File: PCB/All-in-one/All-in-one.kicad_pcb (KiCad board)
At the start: 2 copper layers, 4 parts, among them U1 MPU6050, U2 BMP280, U3 NEO-6M-GPS, U4 STM32F401CCUx

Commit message: Updated PCB Layout
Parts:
- added C1: 10u, Capacitor_SMD:C_1206_3216Metric, F.Cu at (161.7, 63.9)
- added C10: 1u, Capacitor_SMD:C_0603_1608Metric, F.Cu at (134.9, 64.2)
- added C11: 10n, Capacitor_SMD:C_0402_1005Metric, F.Cu at (133.5, 64.4)
- added C12: 4u7, Capacitor_SMD:C_0603_1608Metric, F.Cu at (134.6, 55.3)
- added C13: 100n, Capacitor_SMD:C_0402_1005Metric, F.Cu at (135.1, 57.2)
- added C14: 100n, Capacitor_SMD:C_0402_1005Metric, F.Cu at (143.5, 65.3)
- added C15: 100n, Capacitor_SMD:C_0402_1005Metric, F.Cu at (144.8, 56.9)
- added C16: 100n, Capacitor_SMD:C_0402_1005Metric, F.Cu at (137.3, 55.6)
- added C17: 12p, Capacitor_SMD:C_0402_1005Metric, F.Cu at (131.8, 57.0)
- added C18: 12p, Capacitor_SMD:C_0402_1005Metric, F.Cu at (131.9, 62.6)
- added C19: 4u7, Capacitor_SMD:C_0603_1608Metric, F.Cu at (141.7, 66.4)
- added C2: 100n, Capacitor_SMD:C_0805_2012Metric, F.Cu at (164.3, 63.9)
- added C20: 10u, Capacitor_SMD:C_0603_1608Metric, F.Cu at (134.5, 43.4)
- added C21: 100n, Capacitor_SMD:C_0402_1005Metric, F.Cu at (134.5, 44.8)
- added C22: 10n, Capacitor_SMD:C_0402_1005Metric, F.Cu at (144.3, 48.8)
- added C23: 100n, Capacitor_SMD:C_0402_1005Metric, F.Cu at (141.5, 44.1)
- added C24: 100n, Capacitor_SMD:C_0402_1005Metric, F.Cu at (144.3, 46.2)
- added C25: 2n2, Capacitor_SMD:C_0402_1005Metric, F.Cu at (137.5, 46.1)
- added C26: 10u, Capacitor_SMD:C_0805_2012Metric, F.Cu at (158.1, 78.8)
- added C27: 10u, Capacitor_SMD:C_0805_2012Metric, F.Cu at (151.7, 76.5)
- added C28: 10u, Capacitor_SMD:C_0805_2012Metric, F.Cu at (154.7, 54.6)
- added C3: 100n, Capacitor_SMD:C_0805_2012Metric, F.Cu at (168.1, 60.6)
- added C4: 22u, Capacitor_SMD:C_1206_3216Metric, F.Cu at (161.5, 58.6)
- added C5: 22u, Capacitor_SMD:C_1206_3216Metric, F.Cu at (164.3, 58.6)
- added C6: 10u, Capacitor_SMD:C_1206_3216Metric, F.Cu at (164.5, 81.2)
- added C7: 100n, Capacitor_SMD:C_0805_2012Metric, F.Cu at (162.1, 80.6)
- added C8: 100n, Capacitor_SMD:C_0805_2012Metric, F.Cu at (159.1, 81.8)
- added C9: 100n, Capacitor_SMD:C_0402_1005Metric, F.Cu at (134.8, 61.6)
- added D1: B5819W, Diode_SMD:D_SOD-123, F.Cu at (157.9, 70.0)
- added D2: LED_BLUE, LED_SMD:LED_0603_1608Metric, F.Cu at (156.1, 76.2)
- added D3: LED_RED, LED_SMD:LED_0603_1608Metric, F.Cu at (159.1, 53.9)
- added D4: LED_GREEN, LED_SMD:LED_0402_1005Metric, F.Cu at (128.8, 24.5)
- added F1: 250mA, Fuse:Fuse_1206_3216Metric, F.Cu at (167.1, 68.2)
- added F2: 250mA, Fuse:Fuse_1206_3216Metric, F.Cu at (162.3, 77.5)
- added FB1: 600 @ 600MHz, Inductor_SMD:L_1206_3216Metric, F.Cu at (163.3, 67.5)
- added H1: MountingHole_Pad, MountingHole:MountingHole_3.5mm_Pad_Via, F.Cu at (189.0, 29.4)
- added H2: MountingHole_Pad, MountingHole:MountingHole_3.5mm_Pad_Via, F.Cu at (166.1, 29.4)
- added H3: MountingHole_Pad, MountingHole:MountingHole_3.5mm_Pad_Via, F.Cu at (177.5, 29.4)
- added H4: MountingHole_Pad, MountingHole:MountingHole_3.5mm_Pad_Via, F.Cu at (200.4, 29.4)
- added J1: HIGH VOLTAGE, TerminalBlock_TE-Connectivity:TerminalBlock_TE_282834-2_1x02_P2.54mm_Horizontal, F.Cu at (176.5, 68.2)
- added J10: SWD, Connector_PinHeader_2.54mm:PinHeader_2x05_P2.54mm_Vertical, F.Cu at (96.2, 63.1)
- added J2: LOW VOLTAGE, TerminalBlock_TE-Connectivity:TerminalBlock_TE_282834-2_1x02_P2.54mm_Horizontal, F.Cu at (169.9, 79.0)
- added J3: Micro_SD_Card_Det, All-in-one-custom:SD_Card_custom, F.Cu at (132.3, 72.6)
- added J4: USB_C_Receptacle_USB2.0, All-in-one-custom:USB_C_16PIN, F.Cu at (152.6, 45.8)
- added J5: GPIO, Connector_PinHeader_2.54mm:PinHeader_1x04_P2.54mm_Vertical, F.Cu at (104.5, 82.0)
- added J6: Conn_01x02, Connector_PinHeader_2.54mm:PinHeader_1x02_P2.54mm_Vertical, F.Cu at (107.0, 74.4)
- added J7: Conn_01x02, Connector_PinHeader_2.54mm:PinHeader_1x02_P2.54mm_Vertical, F.Cu at (107.0, 79.5)
- added J8: I2C_EXT, Connector_PinHeader_2.54mm:PinHeader_1x04_P2.54mm_Vertical, F.Cu at (153.4, 22.1)
- added J9: UART_EXT, Connector_PinHeader_2.54mm:PinHeader_1x04_P2.54mm_Vertical, F.Cu at (110.8, 70.6)
- added L1: 2u2, All-in-one-custom:SMNR4020-2.2UH, F.Cu at (157.7, 63.8)
- added L2: 39n, Inductor_SMD:L_0402_1005Metric, F.Cu at (132.4, 64.5)
- added Q1: AO3401A, Package_TO_SOT_SMD:SOT-23, F.Cu at (170.5, 68.2)
- added R1: 33k, Resistor_SMD:R_0603_1608Metric, F.Cu at (170.5, 58.5)
- added R10: 2k2, Resistor_SMD:R_0603_1608Metric, F.Cu at (141.5, 52.9)
- added R11: 10k, Resistor_SMD:R_0402_1005Metric, F.Cu at (127.1, 73.0)
- added R12: 5k1, Resistor_SMD:R_0402_1005Metric, F.Cu at (150.8, 47.8)
- added R13: 5k1, Resistor_SMD:R_0402_1005Metric, F.Cu at (155.8, 47.8)
- added R14: 10k, Resistor_SMD:R_0603_1608Metric, F.Cu at (155.5, 81.7)
- added R15: 13k, Resistor_SMD:R_0603_1608Metric, F.Cu at (151.9, 80.8)
- added R16: 1k, Resistor_SMD:R_0603_1608Metric, F.Cu at (156.7, 53.0)
- added R17: 10k, Resistor_SMD:R_0603_1608Metric, F.Cu at (157.9, 59.0)
- added R18: 13k, Resistor_SMD:R_0603_1608Metric, F.Cu at (154.9, 58.0)
- added R2: 200, Resistor_SMD:R_0603_1608Metric, F.Cu at (171.2, 61.2)
- added R3: 10k, Resistor_SMD:R_0603_1608Metric, F.Cu at (171.2, 64.7)
- added R4: 1k5, Resistor_SMD:R_0603_1608Metric, F.Cu at (153.7, 75.5)
- added R5: 10k, Resistor_SMD:R_0402_1005Metric, F.Cu at (137.3, 54.4)
- added R6: 510, Resistor_SMD:R_0402_1005Metric, F.Cu at (134.8, 60.4)
- added R7: 1k, Resistor_SMD:R_0603_1608Metric, F.Cu at (136.6, 27.3)
- added R8: 10k, Resistor_SMD:R_0402_1005Metric, F.Cu at (117.3, 81.4)
- added R9: 2k2, Resistor_SMD:R_0603_1608Metric, F.Cu at (138.2, 52.9)
- added SW1: SW_DP3T, All-in-one-custom:K3-2336D-F1, F.Cu at (169.9, 75.0)
- added SW2: SW_Push, All-in-one-custom:GT-TC029, F.Cu at (124.7, 63.3)
- added SW3: SW_Push, All-in-one-custom:GT-TC029, F.Cu at (121.1, 70.4)
- added U5: MPU-6050, Sensor_Motion:InvenSense_QFN-24_4x4mm_P0.5mm, F.Cu at (140.9, 47.5)
- added U6: USBLC6-2P6, Package_TO_SOT_SMD:SOT-666, F.Cu at (153.4, 49.2)
- added U7: MT9700, Package_TO_SOT_SMD:SOT-23-5, F.Cu at (154.9, 78.8)
- added U8: MT9700, Package_TO_SOT_SMD:SOT-23-5, F.Cu at (157.9, 56.5)
- added Y1: 25MHz 12pF, Crystal:Crystal_SMD_3225-4Pin_3.2x2.5mm, F.Cu at (131.9, 59.9)
- U1: value MPU6050 -> TPS563201DDCR; footprint MPU:IC_MPU6050 -> Package_TO_SOT_SMD:SOT-23-6
- U2: value BMP280 -> NCP114AMX330TCG; footprint BMP:XDCR_BMP280 -> Package_DFN_QFN:UDFN-4-1EP_1x1mm_P0.65mm_EP0.48x0.48mm
- U3: value NEO-6M-GPS -> STM32F401CDUx; footprint NEO6M:XCVR_NEO-6M-GPS -> Package_DFN_QFN:QFN-48-1EP_7x7mm_P0.5mm_EP5.6x5.6mm
- U4: value STM32F401CCUx -> BMP280; footprint Package_DFN_QFN:QFN-48-1EP_7x7mm_P0.5mm_EP5.6x5.6mm -> Package_LGA:Bosch_LGA-8_2x2.5mm_P0.65mm_ClockwisePinNumbering
- moved U1 72.3 mm to (167.9, 63.9)
- moved U2 65.0 mm to (160.1, 79.8), turned to 90 degrees
- moved U4 44.8 mm to (134.7, 46.8), turned to 180 degrees
- moved U3 18.3 mm to (140.0, 60.4)
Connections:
- U1 pad 1: unconnected-(U1-Pad1) -> GND
- U1 pad 2: unconnected-(U1-Pad2) -> BUCK_SW
- U1 pad 3: unconnected-(U1-Pad3) -> Net-(C2-Pad1)
- U1 pad 4: unconnected-(U1-Pad4) -> BUCK_VFB
- U1 pad 5: unconnected-(U1-Pad5) -> Net-(C2-Pad1)
- U1 pad 6: unconnected-(U1-Pad6) -> BUCK_VBST
- U2 pad 1: Net-(U2-Pad1) -> Net-(C8-Pad1)
- U2 pad 2: unconnected-(U2-Pad2) -> GND
- U2 pad 3: unconnected-(U2-Pad3) -> Net-(U2-Pad3)
- U2 pad 4: unconnected-(U2-Pad4) -> Net-(U2-Pad3)
- U2 pad 5: unconnected-(U2-Pad5) -> (no net)
- U3 pad 1: (no net) -> +3.3V
- U3 pad 10: Net-(U3-Pad10) -> TIM2_CH1
- U3 pad 12: Net-(U3-Pad10) -> TIM5_CH1
- U3 pad 13: Net-(U3-Pad10) -> unconnected-(U3-Pad13)
- U3 pad 14: unconnected-(U3-Pad14) -> SPI1_NSS
- U3 pad 15: unconnected-(U3-Pad15) -> SPI1_SCK
- U3 pad 16: unconnected-(U3-Pad16) -> SPI1_MISO
- U3 pad 17: unconnected-(U3-Pad17) -> SPI1_MOSI
- U3 pad 18: unconnected-(U3-Pad18) -> SD_CARD_DET
- U3 pad 20: unconnected-(U3-Pad20) -> LED_STATUS
- U3 pad 22: unconnected-(U3-Pad22) -> Net-(C19-Pad1)
- U3 pad 23: unconnected-(U3-Pad23) -> GND
- U3 pad 24: Net-(U3-Pad10) -> +3.3V
- U3 pad 5: unconnected-(U3-Pad5) -> HSE_IN
- U3 pad 6: unconnected-(U3-Pad6) -> HSE_OUT
- U3 pad 7: unconnected-(U3-Pad7) -> NRST
- U3 pad 8: unconnected-(U3-Pad8) -> GND
- U3 pad 9: unconnected-(U3-Pad9) -> +3.3VA
- U4 pad 1: unconnected-(U4-Pad1) -> GND
- U4 pad 2: unconnected-(U4-Pad2) -> +3.3V
- U4 pad 3: unconnected-(U4-Pad3) -> I2C1_SDA
- U4 pad 4: unconnected-(U4-Pad4) -> I2C1_SCL
- U4 pad 5: unconnected-(U4-Pad5) -> GND
- U4 pad 6: unconnected-(U4-Pad6) -> +3.3V
- U4 pad 7: unconnected-(U4-Pad7) -> GND
- U4 pad 8: unconnected-(U4-Pad8) -> +3.3V
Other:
- copper layers 2 -> 4

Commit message: Recovery File
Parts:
- moved D1 16.6 mm to (151.9, 54.6), turned to 90 degrees
- moved U6 0.80 mm to (152.9, 48.6)
- moved R12 0.40 mm to (150.4, 47.8)
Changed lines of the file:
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@@
   )
   (footprint "Package_TO_SOT_SMD:SOT-666" (layer "F.Cu")
-    (at 153.4 49.225 -90)
+    (at 152.9 48.6 -90)
     (descr "SOT666")
     (tags "SOT-666")
@@
       (effects (font (size 1 1) (thickness 0.15)))
     )
-    (fp_rect (start -0.3 0.3) (end 13.1 13.2) (layer "F.SilkS") (width 0.2) (fill none))
+    (fp_rect (start -2.3 -1.6) (end 15.8 13.2) (layer "F.SilkS") (width 0.2) (fill none))
     (pad "" np_thru_hole circle (at 9.65 10.5) (size 0.8 0.8) (drill 0.8) (layers F&B.Cu *.Mask))
     (pad "" np_thru_hole circle (at 1.65 10.5) (size 0.8 0.8) (drill 0.8) (layers F&B.Cu *.Mask))
@@
   )
   (footprint "Resistor_SMD:R_0402_1005Metric" (layer "F.Cu")
-    (at 150.8 47.825 180)
+    (at 150.4 47.825 180)
     (descr "Resistor SMD 0402 (1005 Metric), square (rectangular) end terminal, IPC_7351 nominal, (Body size source: IPC-SM-782 page 72, https://www.pcb-3d.com/wordpress/wp-content/uploads/ipc-sm-782a_amendment_1_and_2.pdf), generated with kicad-footprint-generator")
     (tags "resistor")
@@
   )
   (footprint "Diode_SMD:D_SOD-123" (layer "F.Cu")
-    (at 157.9375 70.05 180)
+    (at 151.9 54.6 90)
     (descr "SOD-123")
     (tags "SOD-123")
@@
     (property "Sheetname" "")
     (attr smd)
-    (fp_text reference "D1" (at 0 -2) (layer "F.SilkS")
-      (effects (font (size 1 1) (thickness 0.15)))
-    )
-    (fp_text value "B5819W" (at 0 2.1) (layer "F.Fab")
-      (effects (font (size 1 1) (thickness 0.15)))
-    )
-    (fp_text user "${REFERENCE}" (at 0 -2) (layer "F.Fab")
+    (fp_text reference "D1" (at 0 -2 90) (layer "F.SilkS")
+      (effects (font (size 1 1) (thickness 0.15)))
+    )
+    (fp_text value "B5819W" (at 0 2.1 90) (layer "F.Fab")
+      (effects (font (size 1 1) (thickness 0.15)))
+    )
+    (fp_text user "${REFERENCE}" (at 0 -2 90) (layer "F.Fab")
       (effects (font (size 1 1) (thickness 0.15)))
     )
@@
     (fp_line (start 0.25 -0.4) (end 0.25 0.4) (layer "F.Fab") (width 0.1))
     (fp_line (start -1.4 -0.9) (end 1.4 -0.9) (layer "F.Fab") (width 0.1))
-    (pad "1" smd rect (at -1.65 0 180) (size 0.9 1.2) (layers "F.Cu" "F.Paste" "F.Mask")
+    (pad "1" smd rect (at -1.65 0 90) (size 0.9 1.2) (layers "F.Cu" "F.Paste" "F.Mask")
       (net 82 "BUCK_VIN") (pinfunction "K") (pintype "passive"))
-    (pad "2" smd rect (at 1.65 0 180) (size 0.9 1.2) (layers "F.Cu" "F.Paste" "F.Mask")
+    (pad "2" smd rect (at 1.65 0 90) (size 0.9 1.2) (layers "F.Cu" "F.Paste" "F.Mask")
       (net 18 "+5V") (pinfunction "A") (pintype "passive"))
     (model "${KICAD6_3DMODEL_DIR}/Diode_SMD.3dshapes/D_SOD-123.wrl"

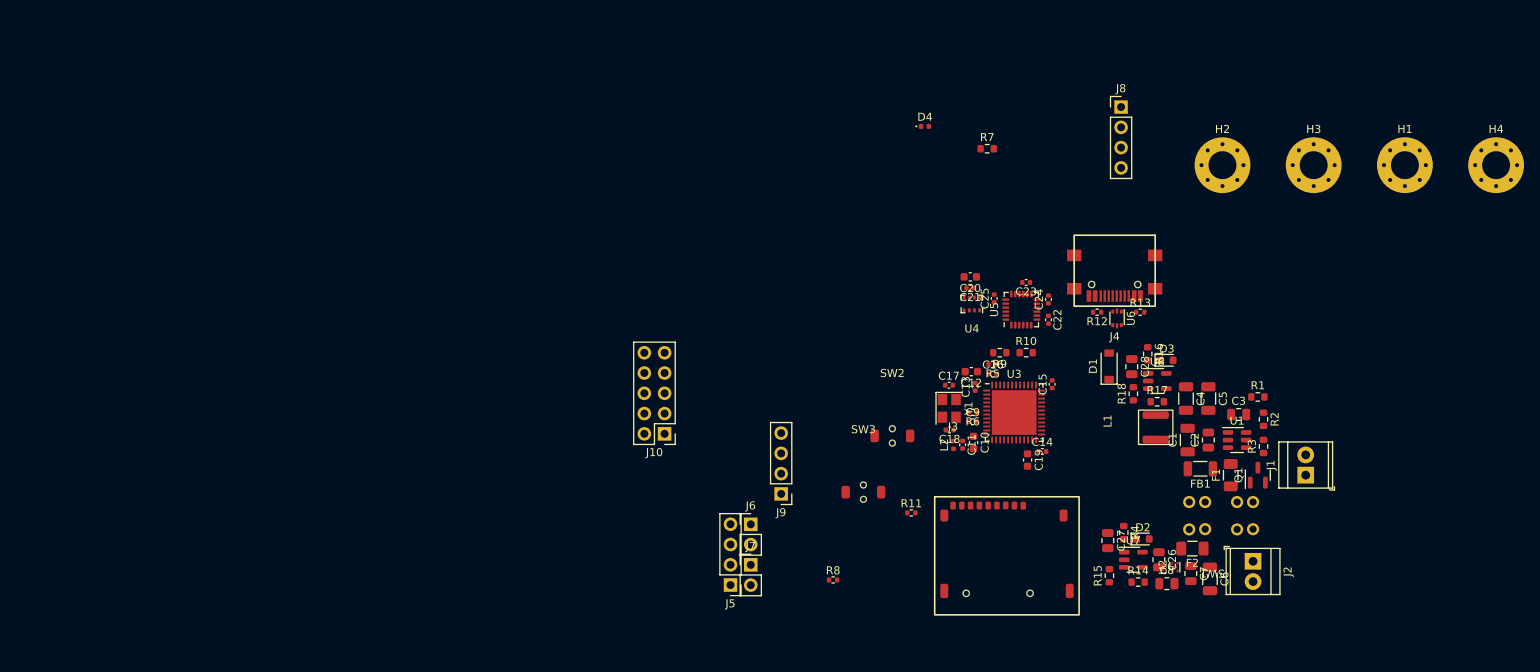
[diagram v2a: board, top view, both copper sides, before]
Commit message: Completed PCB Layout (No Tracing) - Made PCB layout - Tracing need to be done
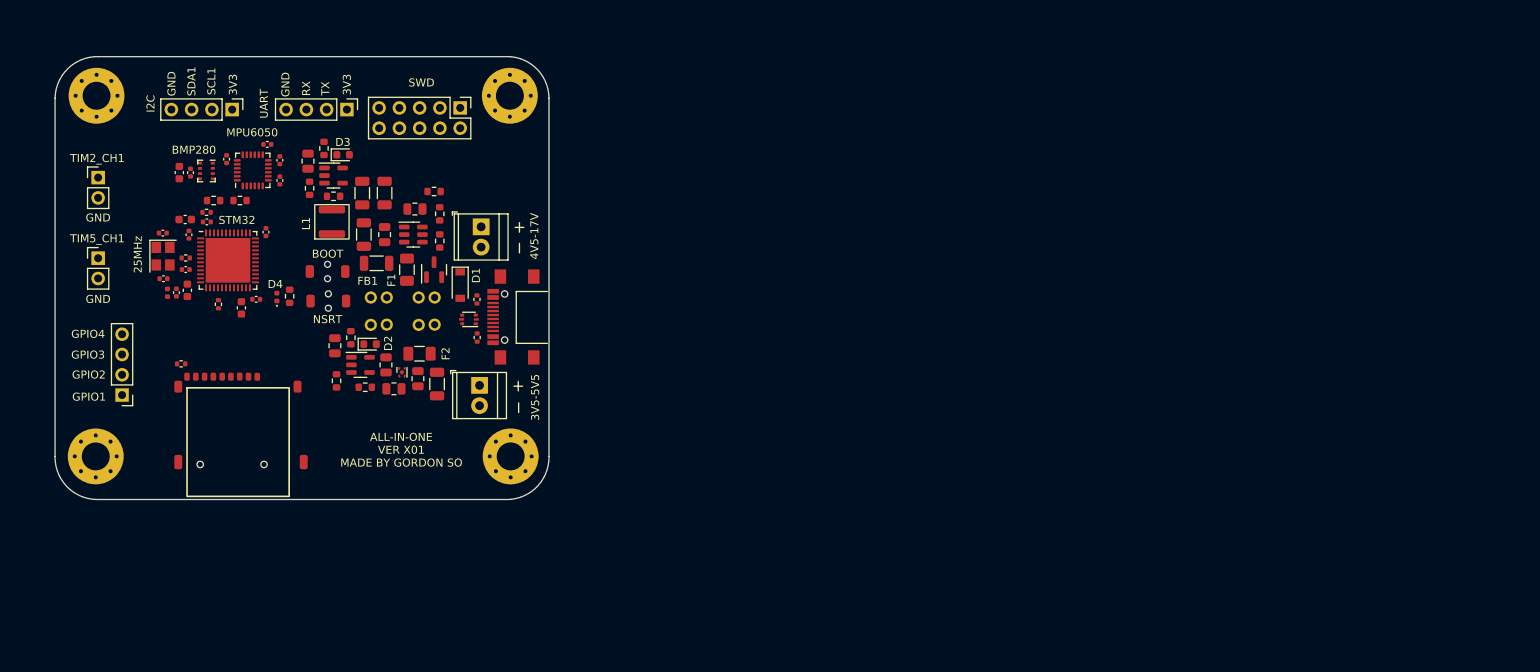
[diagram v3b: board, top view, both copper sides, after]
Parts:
- J5: value GPIO -> GPIO1
- J6: value Conn_01x02 -> TIM2_CH1
- J7: value Conn_01x02 -> TIM5_CH1
- J8: value I2C_EXT -> I2C
- J9: value UART_EXT -> UART
- U5: value MPU-6050 -> MPU6050
- moved H3 156.9 mm to (24.9, 65.9)
- moved H2 141.4 mm to (25.0, 20.7)
- moved H4 128.8 mm to (76.9, 65.9)
- moved H1 112.5 mm to (76.8, 20.7)
- moved J8 111.4 mm to (42.0, 22.4), turned to -90 degrees
- moved J1 107.9 mm to (73.2, 37.1), turned to -90 degrees
- moved C1 106.4 mm to (58.5, 38.1)
- moved C2 106.4 mm to (61.1, 38.1)
- moved C28 106.4 mm to (51.5, 28.9)
- moved C5 106.4 mm to (61.1, 32.9)
- moved FB1 106.4 mm to (60.1, 41.7)
- moved L1 106.4 mm to (54.5, 38.0)
- moved R16 106.4 mm to (53.5, 27.3)
- moved C4 106.4 mm to (58.3, 32.9)
- moved Q1 106.4 mm to (67.3, 42.5)
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- renumbered SW3 to BOOT, U3 to STM32
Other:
- board outline added: 61.9 x 55.5 mm
- rule pad_to_mask_clearance: 0 -> 0.05
- board text added: "25MHz"
- board text added: "3V3"
- board text added: "3V5-5V5"
- board text added: "4V5-17V"
- board text added: "ALL-IN-ONE VER X01 MADE BY GORDON SO"
- board text added: "GND"
- board text added: "GPIO2"
- board text added: "GPIO3"
- board text added: "GPIO4"
- board text added: "JLCJLCJLCJLC"
- board text added: "RX"
- board text added: "SCL1"
- board text added: "SDA1"
- board text added: "TX"

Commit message: Ver X01 PCB Routing Completed -  PCB is completed and all MFG files are exported - gbr files are uploaded to JLCPCB for quoting - All parts needed to be sourced - Encounterd some bug at using CubeIDE
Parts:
- C2: footprint Capacitor_SMD:C_0805_2012Metric -> Capacitor_SMD:C_1206_3216Metric
- D4: footprint LED_SMD:LED_0402_1005Metric -> LED_SMD:LED_0603_1608Metric
- J5: value GPIO1 -> GPIO
- J6: value TIM2_CH1 -> Conn_01x02
- J7: value TIM5_CH1 -> Conn_01x02
- J8: value I2C -> I2C_EXT
- J9: value UART -> UART_EXT
- SW3: renamed from BOOT; value SW_Push -> BOOT
- U5: value MPU6050 -> MPU-6050
- moved SW2 20.9 mm to (33.6, 50.7), turned to 90 degrees
- moved R5 15.1 mm to (52.9, 40.6)
- moved R7 7.95 mm to (50.9, 53.6), turned to -90 degrees
- moved D4 5.80 mm to (50.9, 50.7)
- moved C9 5.02 mm to (32.8, 46.2)
- moved L2 2.69 mm to (36.5, 44.8), turned to 0 degrees
- moved C11 2.17 mm to (36.4, 43.7), turned to 180 degrees
- moved F2 1.93 mm to (63.5, 53.1), turned to -90 degrees
- moved C28 1.64 mm to (52.8, 27.9)
- moved C10 1.63 mm to (36.6, 46.7)
- moved R8 1.48 mm to (40.2, 48.3)
- moved C20 1.35 mm to (34.7, 31.5)
- moved R18 1.32 mm to (53.0, 32.5)
- moved L1 1.20 mm to (55.7, 38.1)
- moved C4 1.20 mm to (59.5, 32.9)
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- renumbered STM32 to U3
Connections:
- J6 pad 1: TIM2_CH1 -> TIM2_CH4
- J7 pad 1: TIM5_CH1 -> TIM3_CH4
- SW1 pad 6: unconnected-(SW1-Pad6) -> LDO_IN
- SW1 pad 8: LDO_IN -> unconnected-(SW1-Pad8)
- U3 pad 10: TIM2_CH1 -> unconnected-(U3-Pad10)
- U3 pad 12: TIM5_CH1 -> unconnected-(U3-Pad12)
- U3 pad 13: unconnected-(U3-Pad13) -> TIM2_CH4
- U3 pad 19: unconnected-(U3-Pad19) -> TIM3_CH4
- U3 pad 20: LED_STATUS -> unconnected-(U3-Pad20)
- U3 pad 29: unconnected-(U3-Pad29) -> LED_STATUS
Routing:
- net GND: track 0.00 -> 161.5 mm, vias 0 -> 100
- net NRST: track 0.00 -> 73.4 mm
- net GPIO_4: track 0.00 -> 56.8 mm, vias 0 -> 1
- net +3.3V: track 0.00 -> 51.7 mm, vias 0 -> 24
- net GPIO_3: track 0.00 -> 50.5 mm, vias 0 -> 1
- net GPIO_2: track 0.00 -> 43.5 mm, vias 0 -> 1
- net SWDIO: track 0.00 -> 35.8 mm, vias 0 -> 1
- net GPIO_1: track 0.00 -> 33.9 mm, vias 0 -> 1
- net USB_D+: track 0.00 -> 32.1 mm
- net USB_D-: track 0.00 -> 32.1 mm
- net SWCLK: track 0.00 -> 30.7 mm, vias 0 -> 1
- net SWO: track 0.00 -> 29.2 mm, vias 0 -> 1
- net UART2_TX: track 0.00 -> 26.6 mm, vias 0 -> 2
- net LDO_IN: track 0.00 -> 26.5 mm
- net TIM2_CH4: track 0.00 -> 25.8 mm, vias 0 -> 1
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- added copper zone on In2.Cu, net +3.3V
- added copper zone on F.Cu, net GND
- added copper zone on In1.Cu, net GND
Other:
- board text added: "+"
- board text added: "ALL-IN-ONE VER X01 MADE BY GORDON SO 11-SEP-2022"
- board text added: "GPIO1"
- board text added: "NRST"
- board text added: "OFF-LV-HV"
- board text added: "STM32F4"
- board text added: "SWCLK"
- board text added: "SWDIO"
- board text added: "SWO"
- board text added: "TIM2_CH4"
- board text added: "TIM3_CH4"
- board text removed: "ALL-IN-ONE VER X01 MADE BY GORDON SO"

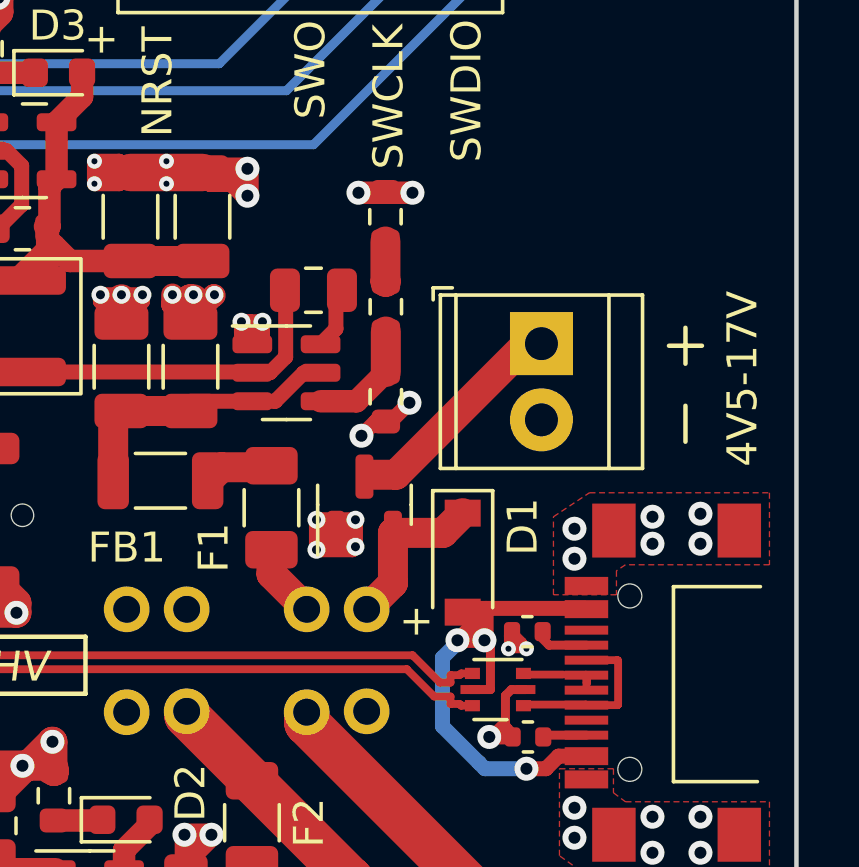
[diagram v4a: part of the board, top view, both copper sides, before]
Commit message: Production Files Updated - Sent to JLCPCB for manufracturing - No SMD parts can be shipped with the order, to reduce the cost, it is most likely that a pre-assembled PCB will be ordered
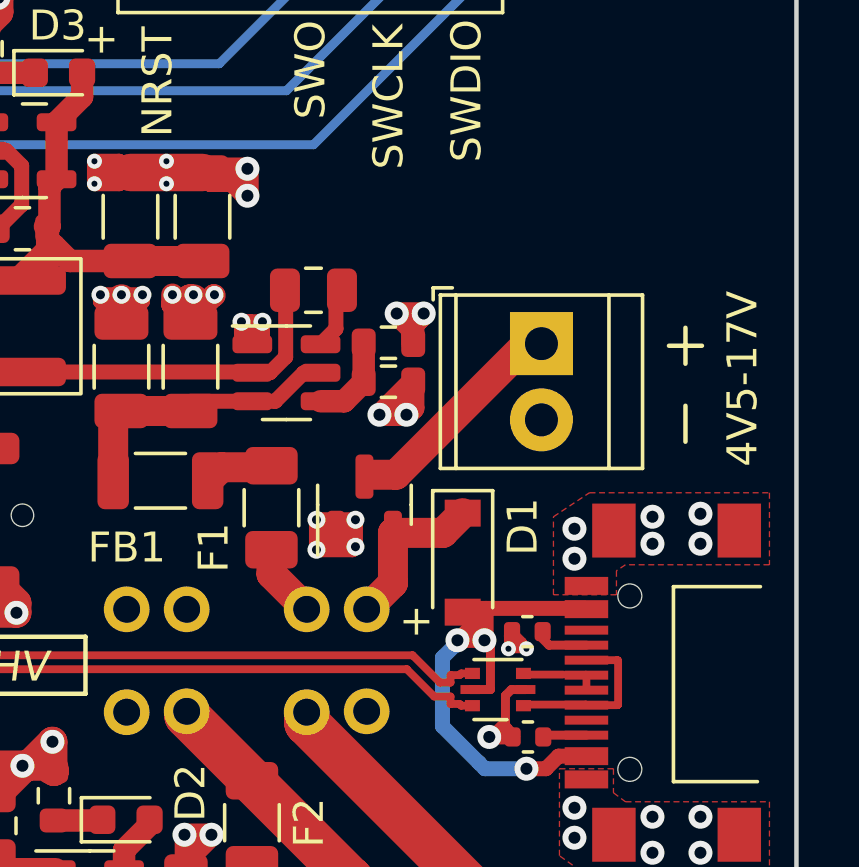
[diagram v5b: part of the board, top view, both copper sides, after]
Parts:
- removed the R2 at (68.0, 35.9)
- FB1: value 600 @ 600MHz -> 600 @ 100MHz
- R1: value 33k -> 33.2k
- moved R1 4.20 mm to (68.1, 37.1), turned to 180 degrees
- moved R2 0.51 mm to (68.1, 38.4), turned to 180 degrees
- renumbered R6 to R10, R7 to R11, R8 to R12, R9 to R13, R10 to R14, R11 to R15, R12 to R16, R13 to R17, R3 to R2, R4 to R3, R14 to R4, R15 to R5, R16 to R6, R17 to R7, R18 to R8, R5 to R9
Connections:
- R1 pad 2: Net-(R1-Pad2) -> BUCK_VFB
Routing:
- net +3.3V: track 51.7 -> 53.6 mm
- net GND: track 161.5 -> 163.1 mm
- net Net-(R1-Pad2): track 1.36 -> 0.00 mm
- net BUCK_VFB: track 3.93 -> 3.01 mm
